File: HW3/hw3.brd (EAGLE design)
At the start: 50 x 50 mm, 23 parts, among them J1 USB-MINIB-5PUSB-MINIB-2SUPPORT, J2 M06, J3 M08_1, J4 M08_2

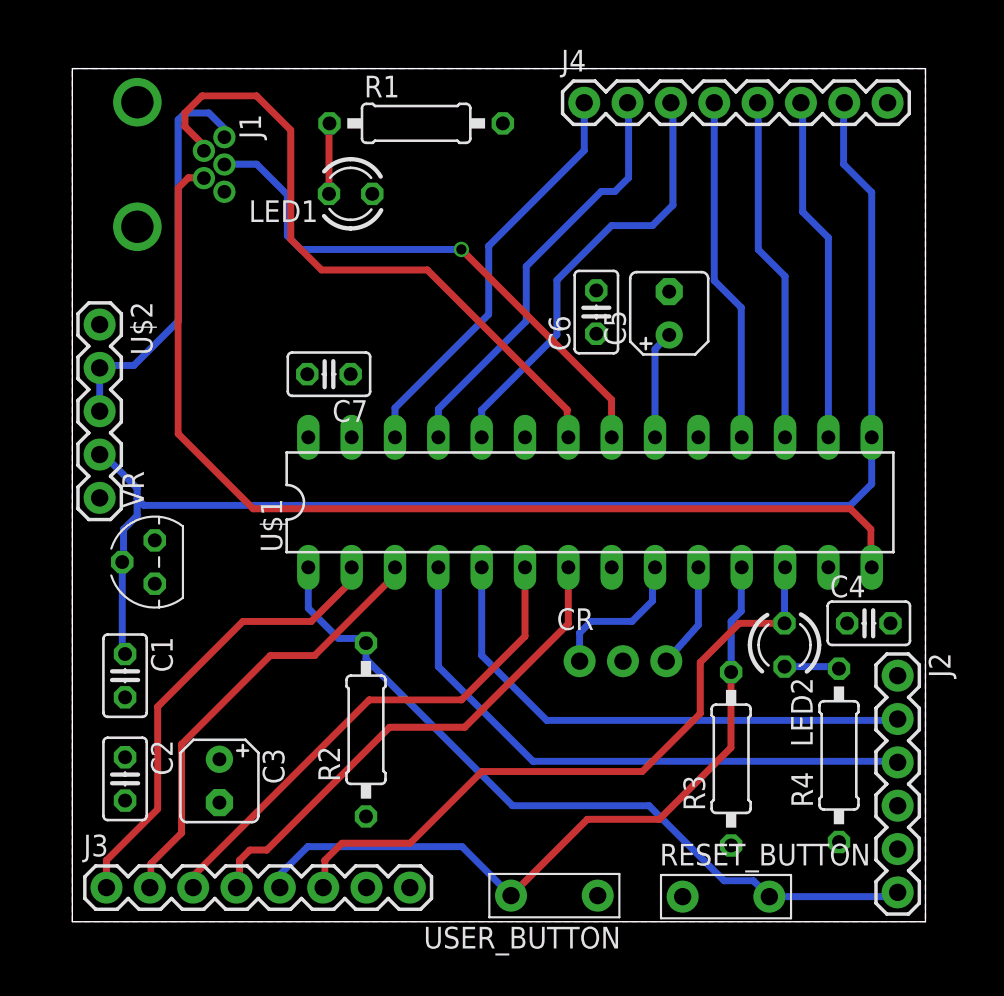
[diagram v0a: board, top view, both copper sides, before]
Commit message: Redesigned schematic and board
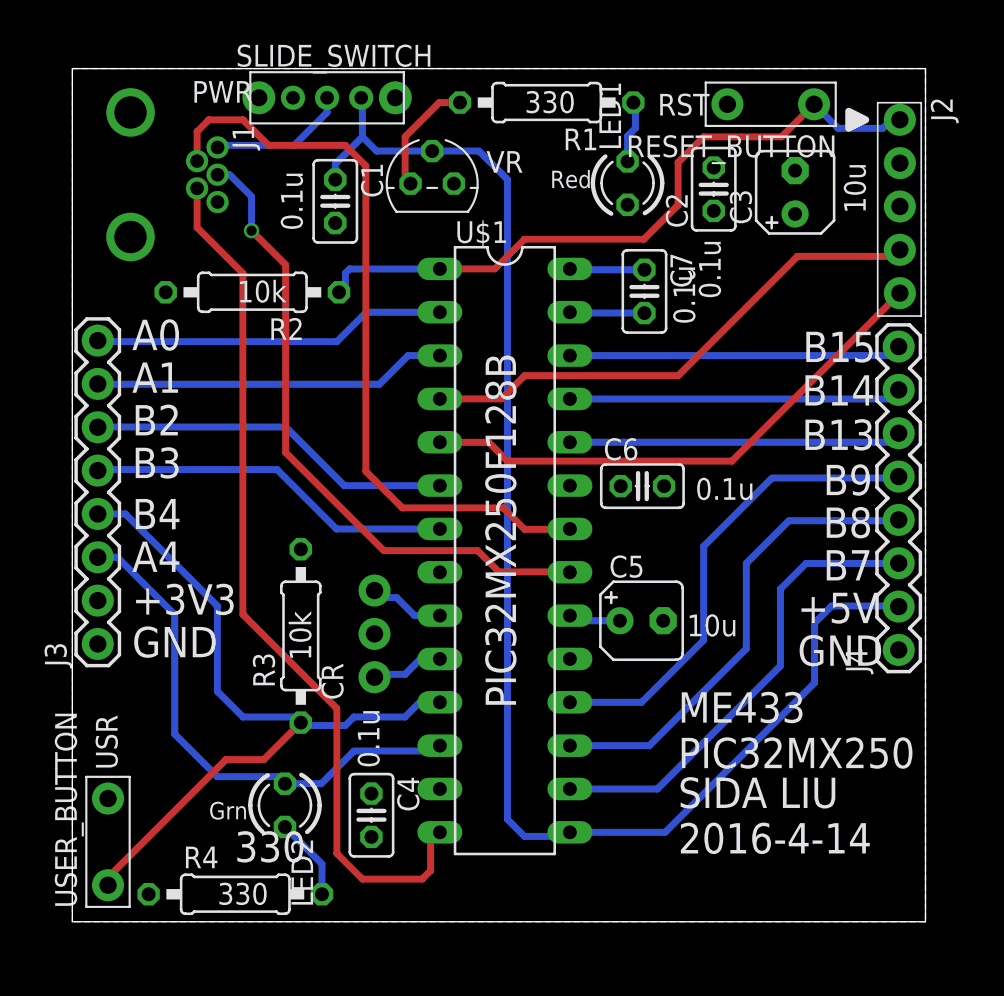
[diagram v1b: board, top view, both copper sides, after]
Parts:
- removed U$2: 1825232-1, hw2:1X05
- added SLIDE_SWITCH: 1825232-1, hw2:1X05_SLIDESWITCH
- J2: value M06 -> M05; device hw2:1X06 -> hw2:1X05_NO_SILK
- J3: value M08_1 -> M08#1
- J4: value M08_2 -> M08#2
- moved C2 48.8 mm to (37.6, 42.9), turned to 90 degrees
- moved C3 48.3 mm to (42.4, 42.8), turned to 90 degrees
- moved RESET_BUTTON 47.1 mm to (43.5, 47.9), turned to 180 degrees
- moved J4 37.0 mm to (48.4, 15.9), turned to 90 degrees
- moved R4 36.3 mm to (9.55, 1.61), turned to 0 degrees
- moved J2 32.6 mm to (48.5, 47.0)
- moved C4 31.2 mm to (17.5, 6.24), turned to 270 degrees
- moved LED2 30.8 mm to (12.5, 6.82)
- moved C1 30.4 mm to (15.4, 42.2)
- moved USER_BUTTON 28.7 mm to (2.09, 2.14), turned to 90 degrees
- moved VR 27.5 mm to (21.1, 43.3), turned to 0 degrees
- moved R2 26.5 mm to (10.6, 36.9), turned to 180 degrees
- moved R3 26.2 mm to (13.4, 16.8)
- moved C7 19.1 mm to (33.5, 36.9), turned to 270 degrees
- moved C5 18.1 mm to (33.4, 17.6), turned to 0 degrees
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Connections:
- net N$1 renamed USBID
- net N$2 renamed D+
- net N$5 renamed D-
- removed net N$10: J3.5, R3.2, U$1.11, USER_BUTTON.2
- removed net N$11: CR.3, U$1.10
- removed net N$12: J3.6, LED2.A, U$1.12
- removed net N$15: J3.1, U$1.2
- removed net N$16: J3.2, U$1.3
- removed net N$17: J3.3, U$1.6
- removed net N$18: J3.4, U$1.7
- removed net N$19: J4.1, U$1.26
- removed net N$20: J4.2, U$1.25
- removed net N$21: J4.3, U$1.24
- removed net N$22: J4.4, U$1.18
- removed net N$23: J4.5, U$1.17
- removed net N$24: J4.6, U$1.16
- removed net N$7: J2.6, R2.2, RESET_BUTTON.2, U$1.1
- removed net N$8: J2.3, U$1.4
- removed net N$9: CR.1, U$1.9
- new net MCLR: J2.1, R2.1, RESET_BUTTON.1, U$1.1
- new net N$5: CR.3, U$1.9
- new net RA0: J3.8, U$1.2
- new net RA1: J3.7, U$1.3
- new net RA4: J3.3, LED2.A, U$1.12
- new net RB0: J2.4, U$1.4
- new net RB1: J2.5, U$1.5
- new net RB13: J4.6, U$1.24
- new net RB14: J4.7, U$1.25
- new net RB15: J4.8, U$1.26
- new net RB2: J3.6, U$1.6
- new net RB3: J3.5, U$1.7
- new net RB4: J3.4, R3.1, U$1.11, USER_BUTTON.1
- new net RB7: J4.3, U$1.16
- new net RB8: J4.4, U$1.17
- new net RB9: J4.5, U$1.18
- net +3V3: now also C7.1, J2.2, J3.2, R2.2, R3.2; no longer C7.2, J2.5, J3.7, R2.1, R3.1
- net +5V: now also J4.2, SLIDE_SWITCH.4; no longer J4.7, U$2.4
- net GND: now also C7.2, J2.3, J3.1, J4.1, RESET_BUTTON.2, USER_BUTTON.2; no longer C7.1, J2.4, J3.8, J4.8, RESET_BUTTON.1, USER_BUTTON.1
- net N$4: now also SLIDE_SWITCH.3; no longer U$2.2, U$2.3
- net N$6: now also CR.1, U$1.10; no longer J2.2, U$1.5
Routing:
- net N$7: track 44.6 -> 0.00 mm
- net RB4: track 0.00 -> 44.2 mm
- net N$10: track 43.9 -> 0.00 mm
- net MCLR: track 0.00 -> 40.1 mm
- net N$12: track 39.5 -> 0.00 mm
- net N$8: track 35.1 -> 0.00 mm
- net RB1: track 0.00 -> 31.5 mm
- net N$17: track 30.9 -> 0.00 mm
- net RB0: track 0.00 -> 30.6 mm
- net RA4: track 0.00 -> 30.6 mm
- net N$18: track 30.0 -> 0.00 mm
- net RB9: track 0.00 -> 28.0 mm
- net RB8: track 0.00 -> 27.7 mm
- net RB7: track 0.00 -> 27.4 mm
- net N$16: track 27.3 -> 0.00 mm
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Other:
- board text added: "+3V3"
- board text added: "+5V"
- board text added: "0.1u"
- board text added: "10k"
- board text added: "10u"
- board text added: "330"
- board text added: "A0"
- board text added: "A1"
- board text added: "A4"
- board text added: "B13"
- board text added: "B14"
- board text added: "B15"
- board text added: "B2"
- board text added: "B3"
- board text added: "B4"
- board text added: "B7"
- board text added: "B8"
- board text added: "B9"
- board text added: "GND"
- board text added: "Grn"
- board text added: "ME433 PIC32MX250"
- board text added: "PIC32MX250F128B"
- board text added: "PWR"
- board text added: "RST"
- board text added: "Red"
- board text added: "SIDA LIU 2016-4-14"
- board text added: "USR"
